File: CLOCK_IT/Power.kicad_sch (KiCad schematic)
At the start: 23 parts, among them U4 AXP2101

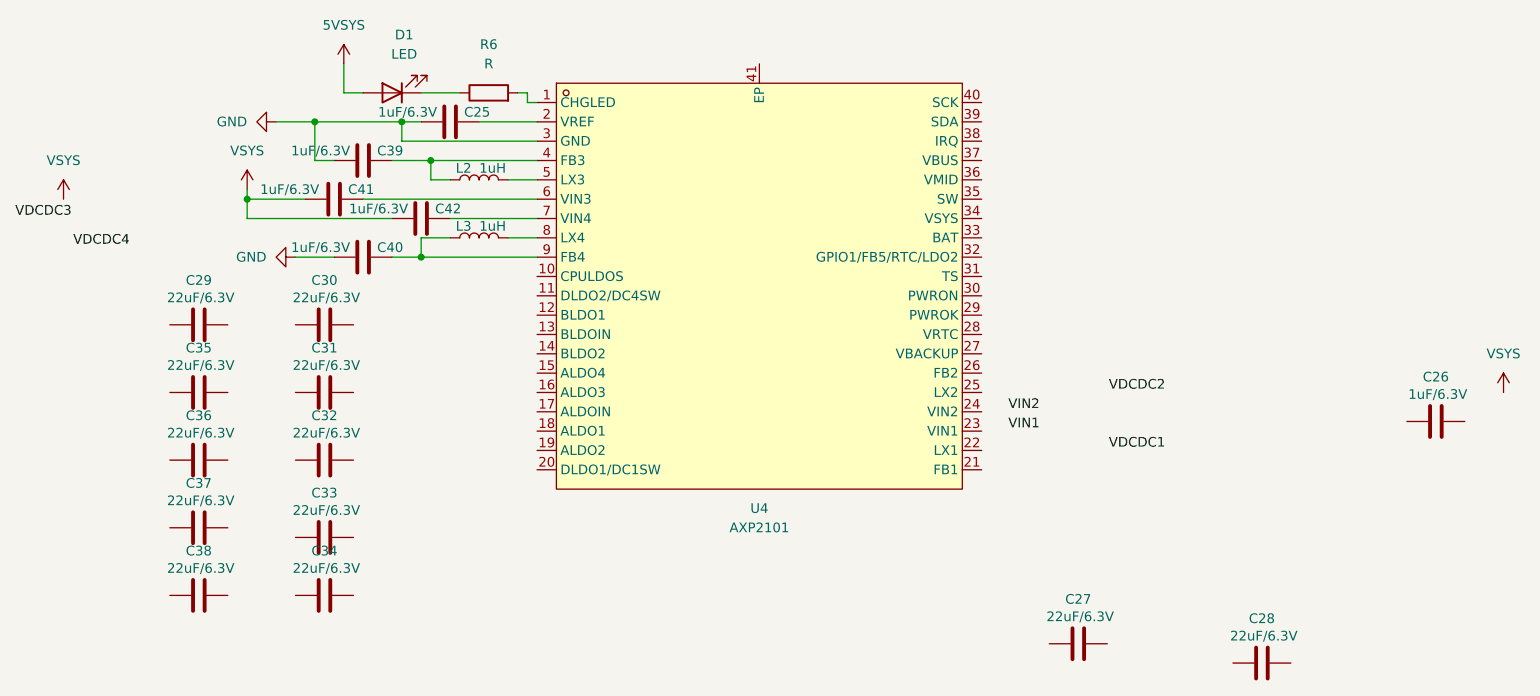
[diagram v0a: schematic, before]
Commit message: :memo: Inpu power Assigning capacitor filters
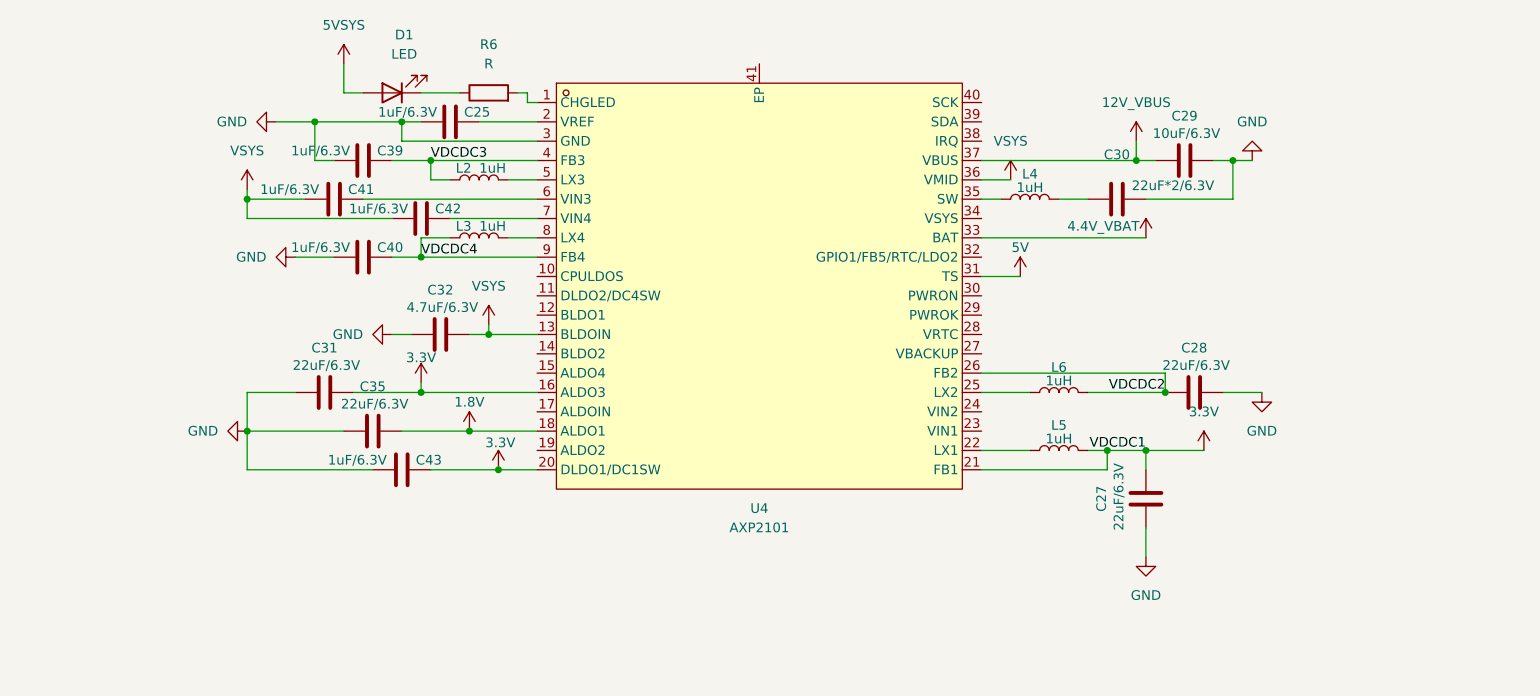
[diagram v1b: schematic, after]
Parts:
- removed C26: 1uF/6.3V, symbol Device:C
- removed C33, C34, C36, C37, C38: 22uF/6.3V, symbol Device:C
- added C43: 1uF/6.3V, symbol Device:C
- added L4, L5, L6: 1uH, symbol Device:L
- C29: value 22uF/6.3V -> 10uF/6.3V
- C30: value 22uF/6.3V -> 22uF*2/6.3V
- C32: value 22uF/6.3V -> 4.7uF/6.3V
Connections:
- net GND: now also C27.1, C28.2, C29.2, C30.2, C31.1, C32.1, C35.1, C43.1
- net VDCDC2: now also C28.1, U4.26 (FB2), L6.2
- net VDCDC3: now also C39.2, L2.1, U4.4 (FB3)
- net VDCDC4: now also C40.2, L3.1, U4.9 (FB4)
- net VSYS: now also C32.2, U4.13 (BLDOIN), U4.36 (VMID)
- net at C30.1: now also L4.2
- net 3.3V: now reaches U4.16 (ALDO3)
- net 3.3V: now also C27.2, C31.2, U4.20 (DLDO1/DC1SW), U4.21 (FB1), C43.2, L5.2
- net 1.8V: now reaches U4.18 (ALDO1)
- net 1.8V: now also C35.2
- net at U4.22 (LX1): now also L5.1
- net at U4.25 (LX2): now also L6.1
- net 5V: now reaches U4.31 (TS)
- net 4.4V_VBAT: now reaches U4.33 (BAT)
- net at U4.35 (SW): now also L4.1
- net 12V_VBUS: now reaches U4.37 (VBUS)
- net 12V_VBUS: now also C29.1
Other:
- moved on the sheet: C27, C28, C29, C30, C32, C35

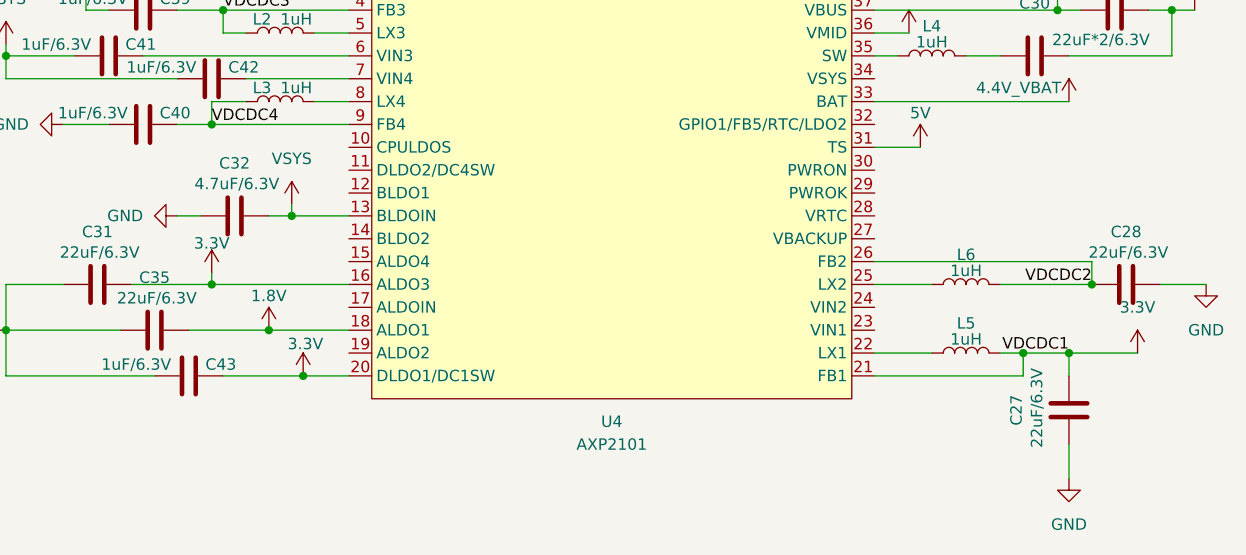
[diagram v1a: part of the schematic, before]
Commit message: :memo: Inpu power Assigning capacitor filters
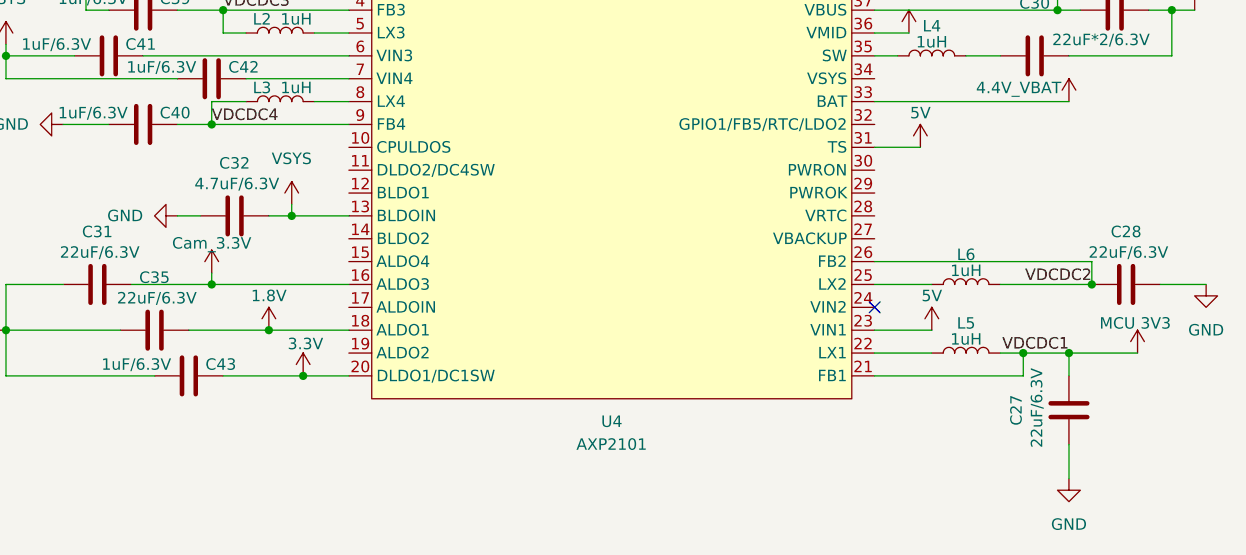
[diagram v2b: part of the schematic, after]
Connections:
- net 3.3V: no longer C27.2, C31.2, L5.2, U4.16 (ALDO3), U4.21 (FB1)
- net 5V: now also U4.23 (VIN1)
- new net Cam_3.3V: C31.2, U4.16 (ALDO3)
- new net MCU 3V3: C27.2, L5.2, U4.21 (FB1)
- no-connect marks 0 -> 1
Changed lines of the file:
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@@
 		(color 0 0 0 0)
 	)
+	(no_connect
+		(at 153.67 83.82)
+	)
 	(wire
 		(pts
@@
 		(pts
 			(xy 81.28 53.34) (xy 81.28 50.8)
+		)
+		(stroke
+			(width 0)
+			(type default)
+		)
+	)
+	(wire
+		(pts
+			(xy 153.67 86.36) (xy 160.02 86.36)
 		)
 		(stroke
@@
 			)
 			(justify right bottom)
-		)
-	)
-	(symbol
-		(lib_id "power:+3.3V")
-		(at 182.88 88.9 0)
-		(unit 1)
-		(exclude_from_sim no)
-		(in_bom yes)
-		(on_board yes)
-		(dnp no)
-		(fields_autoplaced yes)
-		(property "Reference" "#PWR057"
-			(at 182.88 92.71 0)
-			(effects
-				(font
-					(size 1.27 1.27)
-				)
-				(hide yes)
-			)
-		)
-		(property "Value" "3.3V"
-			(at 182.88 83.82 0)
-			(effects
-				(font
-					(size 1.27 1.27)
-				)
-			)
-		)
-		(property "Footprint" ""
-			(at 182.88 88.9 0)
-			(effects
-				(font
-					(size 1.27 1.27)
-				)
-				(hide yes)
-			)
-		)
-		(property "Datasheet" ""
-			(at 182.88 88.9 0)
-			(effects
-				(font
-					(size 1.27 1.27)
-				)
-				(hide yes)
-			)
-		)
-		(property "Description" "Power symbol creates a global label with name \"+3.3V\""
-			(at 182.88 88.9 0)
-			(effects
-				(font
-					(size 1.27 1.27)
-				)
-				(hide yes)
-			)
-		)
-		(pin "1"
-		)
-		(instances
-			(project "CLOCK_IT"
-				(path "/6c8f4e2a-0be1-4eb1-92e1-07339040f4c9/89057fe9-a1d2-4b06-95ab-71c40c05c07f"
-					(reference "#PWR057")
-					(unit 1)
-				)
-			)
 		)
 	)
@@
 	(symbol
 		(lib_id "power:VAA")
+		(at 80.01 80.01 0)
+		(unit 1)
+		(exclude_from_sim no)
+		(in_bom yes)
+		(on_board yes)
+		(dnp no)
+		(property "Reference" "#PWR051"
+			(at 80.01 83.82 0)
+			(effects
+				(font
+					(size 1.27 1.27)
+				)
+				(hide yes)
+			)
+		)
+		(property "Value" "Cam_3.3V"
+			(at 80.01 76.708 0)
+			(effects
+				(font
+					(size 1.27 1.27)
+				)
+			)
+		)
+		(property "Footprint" ""
+			(at 80.01 80.01 0)
+			(effects
+				(font
+					(size 1.27 1.27)
+				)
+				(hide yes)
+			)
+		)
+		(property "Datasheet" ""
+			(at 80.01 80.01 0)
+			(effects
+				(font
+					(size 1.27 1.27)
+				)
+				(hide yes)
+			)
+		)
+		(property "Description" "Power symbol creates a global label with name \"VAA\""
+			(at 80.01 80.01 0)
+			(effects
+				(font
+					(size 1.27 1.27)
+				)
+				(hide yes)
+			)
+		)
+		(pin "1"
+		)
+		(instances
+			(project "CLOCK_IT"
+				(path "/6c8f4e2a-0be1-4eb1-92e1-07339040f4c9/89057fe9-a1d2-4b06-95ab-71c40c05c07f"
+					(reference "#PWR051")
+					(unit 1)
+				)
+			)
+		)
+	)
+	(symbol
+		(lib_id "power:VAA")
 		(at 88.9 72.39 0)
 		(unit 1)
@@
 				(path "/6c8f4e2a-0be1-4eb1-92e1-07339040f4c9/89057fe9-a1d2-4b06-95ab-71c40c05c07f"
 					(reference "#PWR062")
+					(unit 1)
+				)
+			)
+		)
+	)
+	(symbol
+		(lib_id "power:+3.3V")
+		(at 160.02 86.36 0)
+		(unit 1)
+		(exclude_from_sim no)
+		(in_bom yes)
+		(on_board yes)
+		(dnp no)
+		(property "Reference" "#PWR047"
+			(at 160.02 90.17 0)
+			(effects
+				(font
+					(size 1.27 1.27)
+				)
+				(hide yes)
+			)
+		)
+		(property "Value" "5V"
+			(at 160.02 82.55 0)
+			(effects
+				(font
+					(size 1.27 1.27)
+				)
+			)
+		)
+		(property "Footprint" ""
+			(at 160.02 86.36 0)
+			(effects
+				(font
+					(size 1.27 1.27)
+				)
+				(hide yes)
+			)
+		)
+		(property "Datasheet" ""
+			(at 160.02 86.36 0)
+			(effects
+				(font
+					(size 1.27 1.27)
+				)
+				(hide yes)
+			)
+		)
+		(property "Description" "Power symbol creates a global label with name \"+3.3V\""
+			(at 160.02 86.36 0)
+			(effects
+				(font
+					(size 1.27 1.27)
+				)
+				(hide yes)
+			)
+		)
+		(pin "1"
+		)
+		(instances
+			(project "CLOCK_IT"
+				(path "/6c8f4e2a-0be1-4eb1-92e1-07339040f4c9/89057fe9-a1d2-4b06-95ab-71c40c05c07f"
+					(reference "#PWR047")
 					(unit 1)
 				)
@@
 	)
 	(symbol
+		(lib_id "power:VAA")
+		(at 182.88 88.9 0)
+		(unit 1)
+		(exclude_from_sim no)
+		(in_bom yes)
+		(on_board yes)
+		(dnp no)
+		(property "Reference" "#PWR056"
+			(at 182.88 92.71 0)
+			(effects
+				(font
+					(size 1.27 1.27)
+				)
+				(hide yes)
+			)
+		)
+		(property "Value" "MCU 3V3"
+			(at 182.626 85.598 0)
+			(effects
+				(font
+					(size 1.27 1.27)
+				)
+			)
+		)
+		(property "Footprint" ""
+			(at 182.88 88.9 0)
+			(effects
+				(font
+					(size 1.27 1.27)
+				)
+				(hide yes)
+			)
+		)
+		(property "Datasheet" ""
+			(at 182.88 88.9 0)
+			(effects
+				(font
+					(size 1.27 1.27)
+				)
+				(hide yes)
+			)
+		)
+		(property "Description" "Power symbol creates a global label with name \"VAA\""
+			(at 182.88 88.9 0)
+			(effects
+				(font
+					(size 1.27 1.27)
+				)
+				(hide yes)
+			)
+		)
+		(pin "1"
+		)
+		(instances
+			(project "CLOCK_IT"
+				(path "/6c8f4e2a-0be1-4eb1-92e1-07339040f4c9/89057fe9-a1d2-4b06-95ab-71c40c05c07f"
+					(reference "#PWR056")
+					(unit 1)
+				)
+			)
+		)
+	)
+	(symbol
 		(lib_id "Device:C")
 		(at 77.47 91.44 90)
@@
 					(unit 1)
 				)
-			)
-		)
-	)
-	(symbol
-		(lib_id "power:+3.3V")
-		(at 80.01 80.01 0)
-		(unit 1)
-		(exclude_from_sim no)
-		(in_bom yes)
-		(on_board yes)
-		(dnp no)
-		(property "Reference" "#PWR056"
-			(at 80.01 83.82 0)
-			(effects
-				(font
-					(size 1.27 1.27)
-				)
-				(hide yes)
-			)
-		)
-		(property "Value" "3.3V"
-			(at 80.01 76.708 0)
-			(effects
-				(font
-					(size 1.27 1.27)
-				)
-			)
-		)
-		(property "Footprint" ""
-			(at 80.01 80.01 0)
-			(effects
-				(font
-					(size 1.27 1.27)
-				)
-				(hide yes)
-			)
-		)
-		(property "Datasheet" ""
-			(at 80.01 80.01 0)
-			(effects
-				(font
-					(size 1.27 1.27)
-				)
-				(hide yes)
-			)
-		)
-		(property "Description" "Power symbol creates a global label with name \"+3.3V\""
-			(at 80.01 80.01 0)
-			(effects
-				(font
-					(size 1.27 1.27)
-				)
-				(hide yes)
-			)
-		)
-		(pin "1"
-		)
-		(instances
-			(project "CLOCK_IT"
-				(path "/6c8f4e2a-0be1-4eb1-92e1-07339040f4c9/89057fe9-a1d2-4b06-95ab-71c40c05c07f"
-					(reference "#PWR056")
-					(unit 1)
-				)

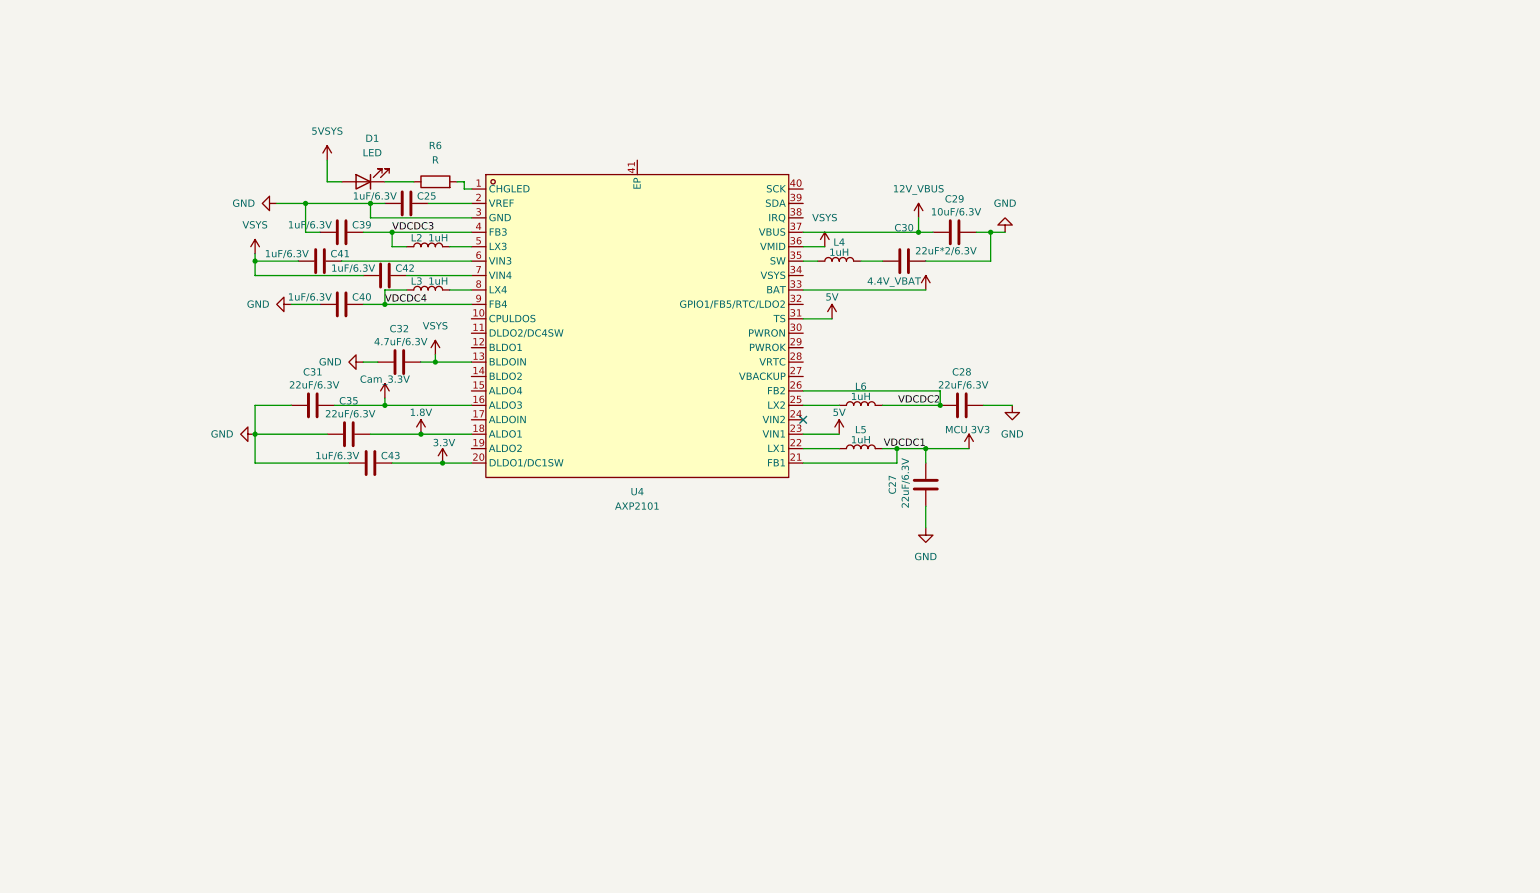
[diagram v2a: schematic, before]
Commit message: :fire: adding I2C communication
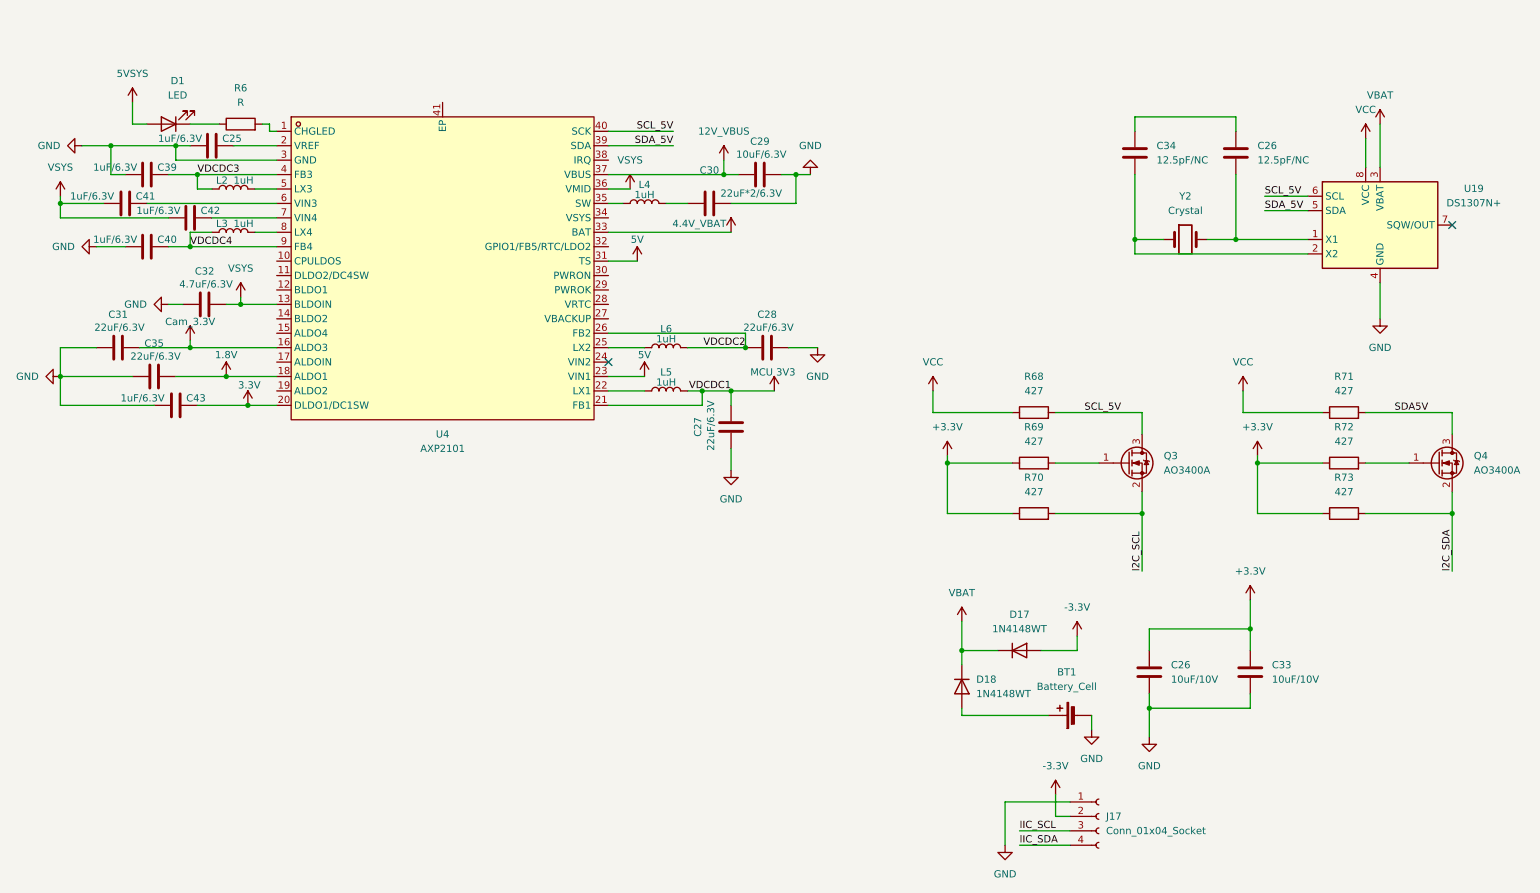
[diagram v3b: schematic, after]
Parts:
- added BT1: Battery_Cell, Battery:BatteryHolder_MPD_BH-18650-PC2, symbol Device:Battery_Cell
- added C26, C33: 10uF/10V, Capacitor_Tantalum_SMD:CP_EIA-2012-12_Kemet-R, symbol Device:C
- added C26, C34: 12.5pF/NC, Capacitor_Tantalum_SMD:CP_EIA-2012-12_Kemet-R, symbol Device:C
- added D17, D18: 1N4148WT, Diode_SMD:D_SOD-523, symbol Diode:1N4148WT
- added J17: Conn_01x04_Socket, Module:Flipper_Zero_Angled, symbol Connector:Conn_01x04_Socket
- added Q3, Q4: AO3400A, Package_TO_SOT_SMD:SOT-23, symbol Transistor_FET:AO3400A
- added R68, R69, R70, R71, R72, R73: 427, Resistor_SMD:R_01005_0402Metric_Pad0.57x0.30mm_HandSolder, symbol Device:R
- added U19: DS1307N+, Package_DIP:DIP-8_W7.62mm, symbol Timer_RTC:DS1307N+
- added Y2: Crystal, Oscillator:Oscillator_SMD_Fox_FT5H_5.0x3.2mm, symbol Device:Crystal
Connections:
- net GND: now also BT1.2 (-), C26.2, C33.2, J17.1 (Pin_1), U19.4 (GND)
- net SDA_5V: now reaches U4.39 (SDA)
- net SDA_5V: now also U19.5 (SDA)
- net SCL_5V: now reaches U4.40 (SCK)
- net SCL_5V: now also Q3.3 (D), R68.2, U19.6 (SCL)
- new net: C26.1, C34.1
- new net: C34.2, U19.2 (X2), Y2.1
- new net: BT1.1 (+), D18.2 (A)
- new net: C26.2, U19.1 (X1), Y2.2
- new net: Q4.1 (G), R72.2
- new net: Q3.1 (G), R69.2
- new net +3.3V: C26.1, C33.1, R69.1, R70.1, R72.1, R73.1
- new net -3.3V: D17.2 (A), J17.2 (Pin_2)
- new net I2C_SCL: Q3.2 (S), R70.2
- new net I2C_SDA: Q4.2 (S), R73.2
- new net IIC_SCL: J17.3 (Pin_3)
- new net IIC_SDA: J17.4 (Pin_4)
- new net SDA5V: Q4.3 (D), R71.2
- new net VBAT: D17.1 (K), D18.1 (K), U19.3 (VBAT)
- new net VCC: R68.1, R71.1, U19.8 (VCC)
- no-connect marks 1 -> 2
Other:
- moved on the sheet: C25, C27, C28, C29, C30, C31, C32, C35, C39, C40, C41, C42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
